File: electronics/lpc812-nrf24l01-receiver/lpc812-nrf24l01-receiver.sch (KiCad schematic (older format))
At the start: 21 parts, among them K1 BAT, K2 CH3, K3 TH, K4 ST, P1 NRF24L01+, SW1 BIND/ISP, U1 MCP1703, U2 LPC812, X1 16MHz

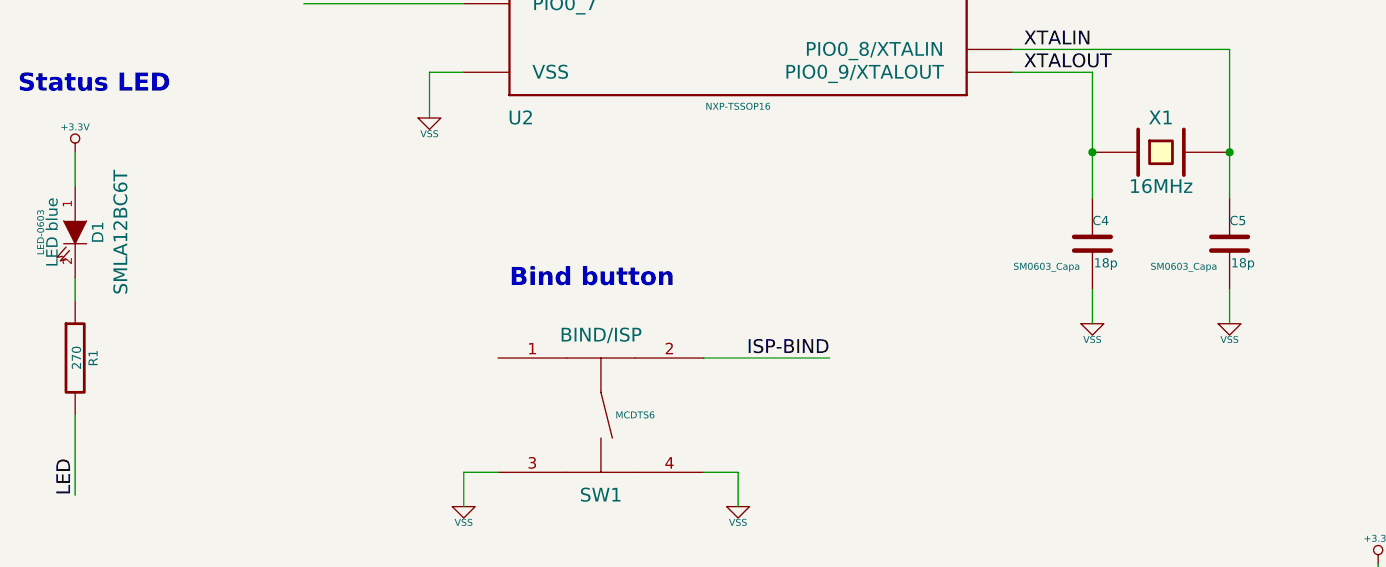
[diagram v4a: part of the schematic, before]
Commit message: Change components to 0805 which we have in stock
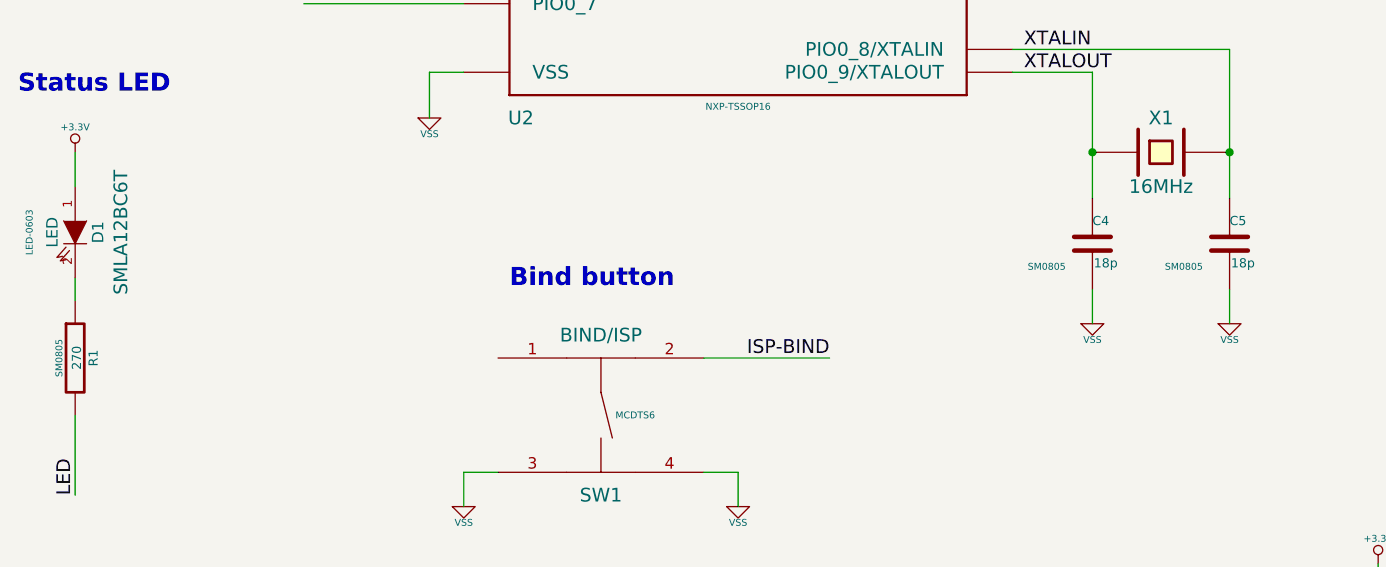
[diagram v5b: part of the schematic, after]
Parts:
- C4, C5: footprint SM0603_Capa -> SM0805
- D1: value LED blue -> LED
- R1: footprint SM0603 -> SM0805
- X1: footprint crystal-SM49 -> Q_49U3HMS
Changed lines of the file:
@@
 F 0 "X1" H 6450 3600 60  0000 C CNN
 F 1 "16MHz" H 6450 3300 60  0000 C CNN
-F 2 "crystal-SM49" H 6450 3450 60  0001 C CNN
+F 2 "Q_49U3HMS" H 6450 3450 60  0001 C CNN
 F 3 "~" H 6450 3450 60  0000 C CNN
 	1    6450 3450
@@
 F 0 "C4" H 6150 3950 40  0000 L CNN
 F 1 "18p" H 6156 3765 40  0000 L CNN
-F 2 "SM0603_Capa" H 5950 3750 30  0000 C CNN
+F 2 "SM0805" H 5950 3750 30  0000 C CNN
 F 3 "~" H 6150 3850 60  0000 C CNN
 	1    6150 3850
@@
 F 0 "C5" H 6750 3950 40  0000 L CNN
 F 1 "18p" H 6756 3765 40  0000 L CNN
-F 2 "SM0603_Capa" H 6550 3750 30  0000 C CNN
+F 2 "SM0805" H 6550 3750 30  0000 C CNN
 F 3 "~" H 6750 3850 60  0000 C CNN
 	1    6750 3850
@@
 P 1700 3800
 F 0 "D1" H 1700 3900 50  0000 C CNN
-F 1 "LED blue" H 1700 3700 50  0000 C CNN
-F 2 "LED-0603" H 1700 3650 30  0000 C CNN
+F 1 "LED" H 1700 3700 50  0000 C CNN
+F 2 "LED-0603" H 1700 3600 30  0000 C CNN
 F 3 "SMLA12BC6T" H 1700 4000 60  0000 C CNN
 	1    1700 3800
@@
 F 0 "R1" V 1780 4350 40  0000 C CNN
 F 1 "270" V 1707 4351 40  0000 C CNN
-F 2 "SM0603" V 1630 4350 30  0001 C CNN
+F 2 "SM0805" V 1630 4350 30  0000 C CNN
 F 3 "~" H 1700 4350 30  0000 C CNN
 	1    1700 4350
